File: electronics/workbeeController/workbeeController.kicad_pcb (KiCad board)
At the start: 2 copper layers, 100 x 100 mm, 88 parts, among them J1 24V, J10 OUT C, J11 OUT D, J12 OUT E, J13 OUT F, J14 OUT G, J15 OUT H, J16 OUT I, J17 OUT J, J18 OUT K, J19 OUT L, J2 SR_OUT_EXT, J20 OUT M, J21 OUT N, J22 OUT O, J23 OUT P, J24 IN A, J25 IN B, J26 IN C, J27 IN D, J28 IN E, J29 IN F, J3 SR_IN_EXT, J30 IN G, J31 IN H, J32 ESTOP, J33 PROBE, J34 RS485, J35 24V, J36 5V, J37 3.3V, J38 GND, J4 PULSE, J5 GND, J6 3.3v, J7 GPIO, J8 OUT A, J9 OUT B, U1 74HC595, U10 PC817, U11 PC817, U12 PC817, U13 PC817, U14 PC817, U15 PC817, U16 PC817, U17 LevelShifterModule, U2 74HC595, U3 TTGO_TDisplay, U4 Buck, U5 74HC165, U6 SP485EN, U7 PC817, U8 PC817, U9 PC817

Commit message: PCB routed
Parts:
- added C6: 0.1uF, Capacitor_THT:C_Disc_D5.0mm_W2.5mm_P2.50mm, F.Cu at (72.3, 73.7)
- added C7: 0.1uF, Capacitor_THT:C_Disc_D5.0mm_W2.5mm_P2.50mm, F.Cu at (41.3, 73.7)
- added H5: MountingHole_Pad, MountingHole:MountingHole_4.3mm_M4_ISO7380_Pad, F.Cu at (35.4, 35.4)
- added J39: IN (INKL), Connector_PinSocket_2.54mm:PinSocket_1x04_P2.54mm_Vertical, F.Cu at (82.5, 73.7)
- added J40: IN (MNOP), Connector_PinSocket_2.54mm:PinSocket_1x04_P2.54mm_Vertical, F.Cu at (74.9, 86.4)
- added U18: 74HC165, Package_DIP:DIP-16_W7.62mm, F.Cu at (69.8, 83.8)
- J10, J11, J12, J13, J14, J15, J16, J17, J18, J19, J20, J21, J22, J23, J24, J25, J26, J27, J28, J29, J30, J31, J32, J33, J8, J9: footprint Connector_PinHeader_2.54mm:PinHeader_1x02_P2.54mm_Vertical -> Connector_PinSocket_2.54mm:PinSocket_1x02_P2.54mm_Vertical
- J35, J36, J37, J38: footprint Connector_PinHeader_2.54mm:PinHeader_1x04_P2.54mm_Vertical -> Connector_PinSocket_2.54mm:PinSocket_1x04_P2.54mm_Vertical
- JP1: value Jumper_NC_Small -> Omit Aux Shift Register (U18); footprint Jumper:SolderJumper-2_P1.3mm_Bridged_Pad1.0x1.5mm -> Jumper:SolderJumper-2_P1.3mm_Open_TrianglePad1.0x1.5mm
- moved U5 25.4 mm to (69.8, 62.2), turned to 90 degrees
- moved J3 23.4 mm to (83.8, 94.0), turned to 270 degrees
- moved JP1 20.7 mm to (88.3, 73.7)
- moved C3 19.3 mm to (72.4, 52.1), turned to 180 degrees
- moved J5 12.0 mm to (27.9, 50.8)
- moved J6 12.0 mm to (30.5, 50.8)
- moved J7 12.0 mm to (33.0, 50.8)
- moved J4 8.52 mm to (33.0, 59.7), turned to 270 degrees
- moved R30 8.03 mm to (31.8, 91.4)
- moved J34 6.48 mm to (34.3, 99.1)
- moved R33 5.24 mm to (108.0, 45.7)
- moved R34 5.24 mm to (95.2, 45.7)
- moved R35 5.24 mm to (82.5, 45.7)
- moved R31 5.08 mm to (34.3, 94.0), turned to 0 degrees
- moved R32 5.08 mm to (39.4, 94.0), turned to 90 degrees
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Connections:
- J3 pad 1: +3V3 -> GND
- J3 pad 5: GND -> +3V3
- JP1 pad 1: /SR_IN_DATA2 -> Net-(JP1-Pad1)
- R15 pad 2: Net-(R15-Pad2) -> +3V3
- R20 pad 2: Net-(R15-Pad2) -> +3V3
- U5 pad 10: /SR_IN_DATA2 -> Net-(JP1-Pad1)
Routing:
- net +3V3: track 0.00 -> 448.5 mm, vias 0 -> 4
- net +5V: track 0.00 -> 230.2 mm, vias 0 -> 2
- net +24V: track 0.00 -> 166.2 mm
- net /SR_OUT_CLOCK: track 0.00 -> 115.1 mm
- net /INT_PROBE: track 0.00 -> 104.2 mm, vias 0 -> 1
- net /SR_OUT_LATCH: track 0.00 -> 100.4 mm, vias 0 -> 2
- net /INT_ESTOP: track 0.00 -> 85.7 mm, vias 0 -> 1
- net /SR_IN_CLOCK: track 0.00 -> 80.6 mm, vias 0 -> 4
- net /SR_OUT_DATA: track 0.00 -> 72.9 mm, vias 0 -> 2
- net /INT_IN_H: track 0.00 -> 71.5 mm
- net /INT_IN_G: track 0.00 -> 64.2 mm
- net /SR_IN_LATCH: track 0.00 -> 59.5 mm, vias 0 -> 2
- net /INT_IN_F: track 0.00 -> 58.0 mm
- net /INT_IN_E: track 0.00 -> 52.9 mm
- net /RS485_RO_3V3: track 0.00 -> 51.7 mm, vias 0 -> 1
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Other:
- net class Power added: clearance 0.3, trace_width 0.35, via_dia 0.8, via_drill 0.4
- board text added: "+"
- board text added: "17"
- board text added: "2"
- board text added: "21"
- board text added: "22"
- board text added: "3.3"
- board text added: "3.3V"
- board text added: "3.3V Aux"
- board text added: "37"
- board text added: "5V"
- board text added: "5v"
- board text added: "A"
- board text added: "Accessory"
- board text added: "B"
- board text added: "C"
- board text added: "D"
- board text added: "E"
- board text added: "ESTOP"
- board text added: "F"
- board text added: "G"
- board text added: "GPIO"
- board text added: "H"
- board text added: "I"
- board text added: "INPUTS"
- board text added: "Isolated 24V"
- board text added: "J"
- board text added: "K"
- board text added: "L"
- board text added: "M"
- board text added: "N"
- board text added: "O"
- board text added: "OUTPUTS"
- board text added: "P"
- board text added: "POWER"
- board text added: "PROBE"
- board text added: "RS485"
- board text added: "Set JP1 if omitting U18"
- board text added: "[Input Expander] Connect D+G if unused"
- board text added: "[Output Expander]"

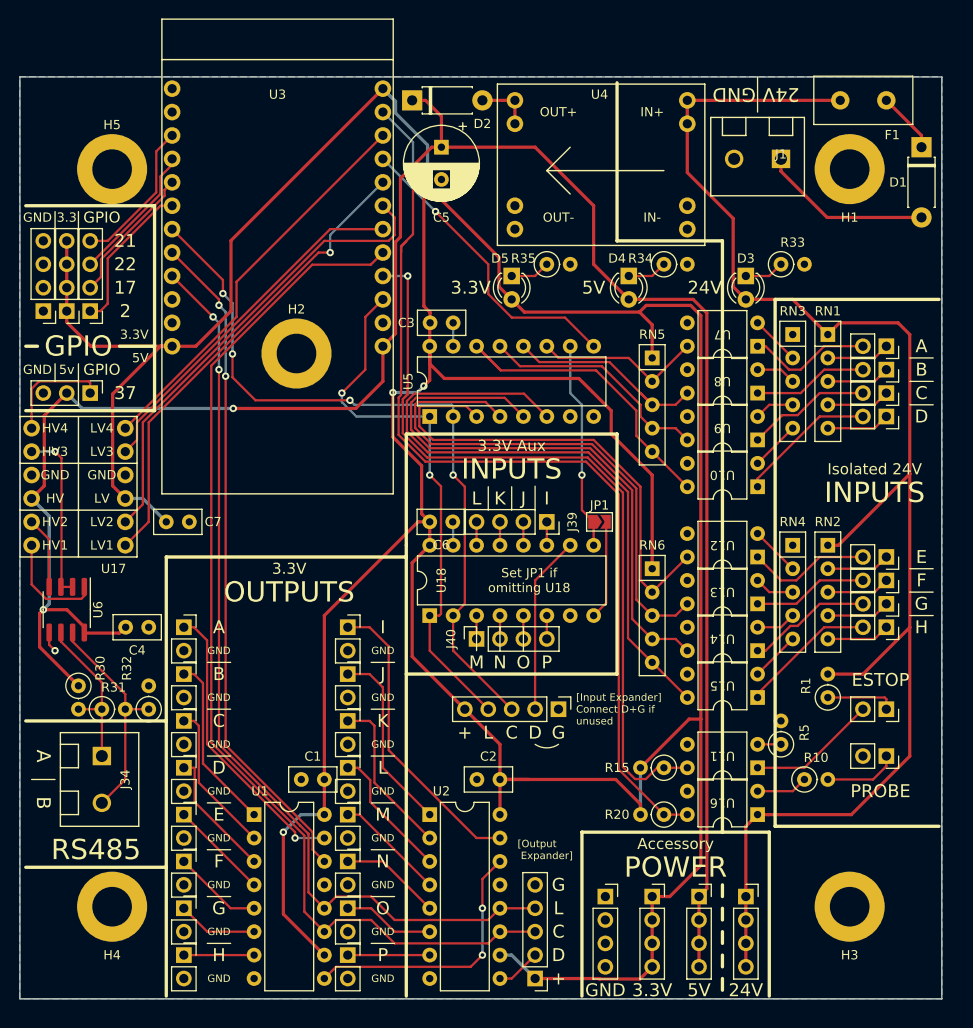
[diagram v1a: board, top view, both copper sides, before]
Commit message: Change resistor footprints, add ground/chassis jumper
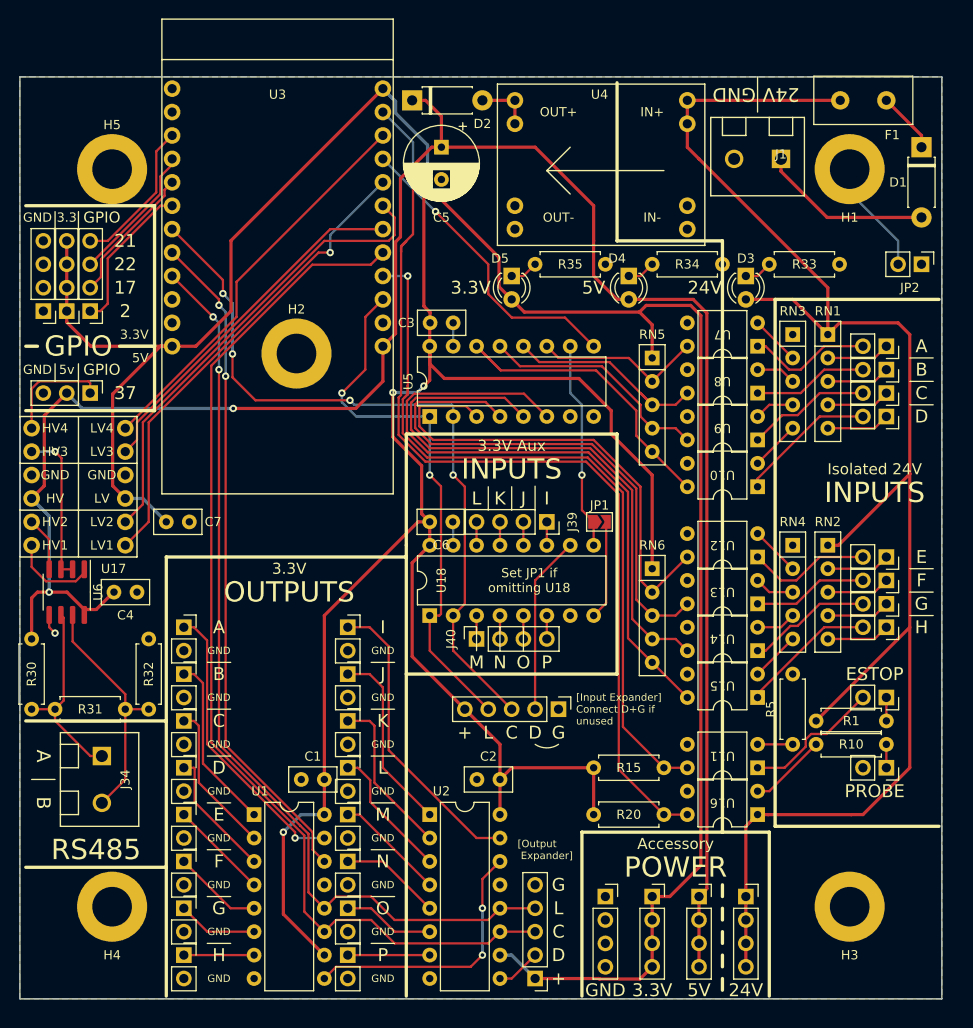
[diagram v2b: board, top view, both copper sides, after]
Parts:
- added JP2: Chassis <=> GND, Connector_PinHeader_2.54mm:PinHeader_1x02_P2.54mm_Vertical, F.Cu at (123.2, 45.7)
- R1, R10, R15, R20, R30, R31, R32, R33, R35, R5: footprint Resistor_THT:R_Axial_DIN0207_L6.3mm_D2.5mm_P2.54mm_Vertical -> Resistor_THT:R_Axial_DIN0207_L6.3mm_D2.5mm_P7.62mm_Horizontal
- R34: value 220 -> 1k; footprint Resistor_THT:R_Axial_DIN0207_L6.3mm_D2.5mm_P2.54mm_Vertical -> Resistor_THT:R_Axial_DIN0207_L6.3mm_D2.5mm_P7.62mm_Horizontal
- moved R30 7.18 mm to (26.7, 86.4)
- moved R1 6.84 mm to (119.4, 95.2), turned to 180 degrees
- moved R31 5.08 mm to (29.2, 94.0)
- moved C4 4.02 mm to (38.1, 81.3)
- moved R10 4.02 mm to (111.8, 97.8)
- moved U6 1.91 mm to (30.5, 81.3)
- moved J32 1.27 mm to (119.4, 92.7)
- moved J33 1.27 mm to (119.4, 100.3)
- moved R33 1.27 mm to (106.7, 45.7)
- moved R34 1.27 mm to (94.0, 45.7)
- moved R35 1.27 mm to (81.3, 45.7)
- moved R5 1.27 mm to (109.2, 97.8)
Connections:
- H1 pad 1: (no net) -> Net-(H1-Pad1)
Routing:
- net +3V3: track 448.5 -> 430.4 mm
- net Net-(H1-Pad1): track 0.00 -> 12.3 mm
- net +24V: track 166.2 -> 177.8 mm
- net +5V: track 230.2 -> 223.2 mm
- net /EXT_PROBE: track 8.05 -> 2.54 mm
- net Net-(J32-Pad1): track 7.52 -> 2.54 mm
- net /INT_ESTOP: track 85.7 -> 82.1 mm
- net /EXT_485_A: track 17.8 -> 21.2 mm
- net Net-(R10-Pad1): track 5.61 -> 8.45 mm
- net /RS485_RO: track 11.7 -> 9.53 mm
- net /RS485_RTS: track 18.7 -> 16.8 mm
- net /RS485_DI: track 7.84 -> 5.93 mm
- net /EXT_485_B: track 24.4 -> 26.3 mm
- net Net-(D4-Pad1): track 4.34 -> 3.07 mm
- net Net-(D3-Pad1): track 4.34 -> 3.07 mm
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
